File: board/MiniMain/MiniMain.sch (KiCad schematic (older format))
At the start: 40 parts

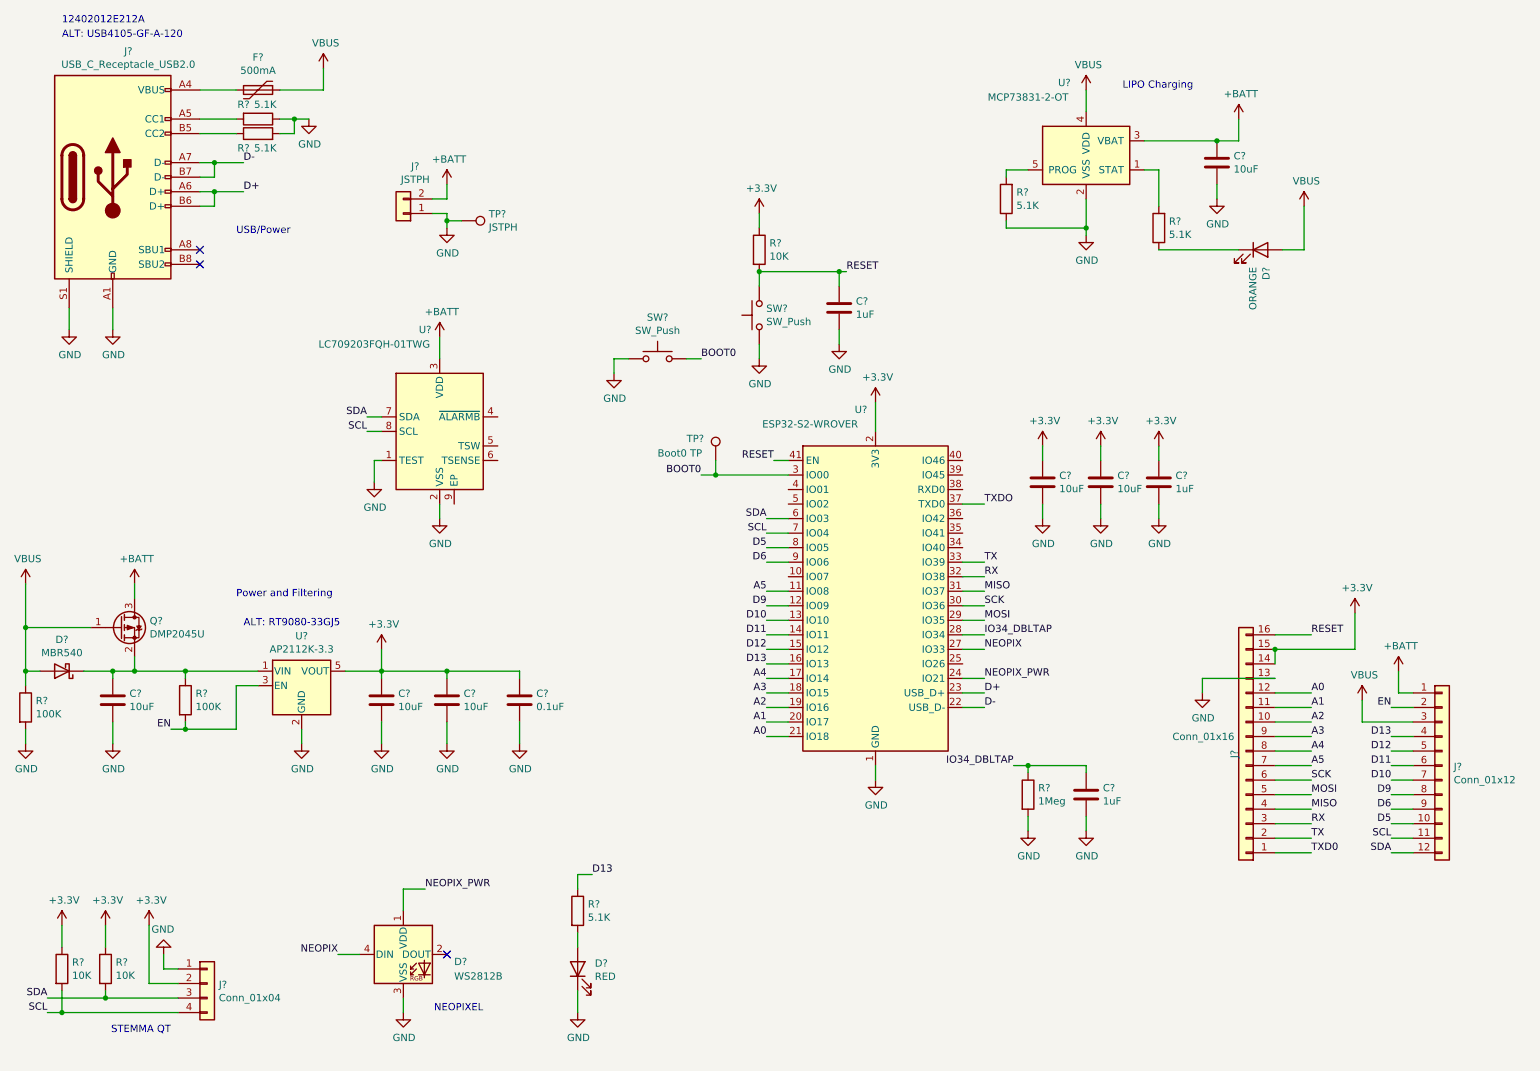
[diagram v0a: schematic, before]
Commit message: Added support for turning power off on the "Stemma QT" port like in the Adafruit esp32-s2 feather.
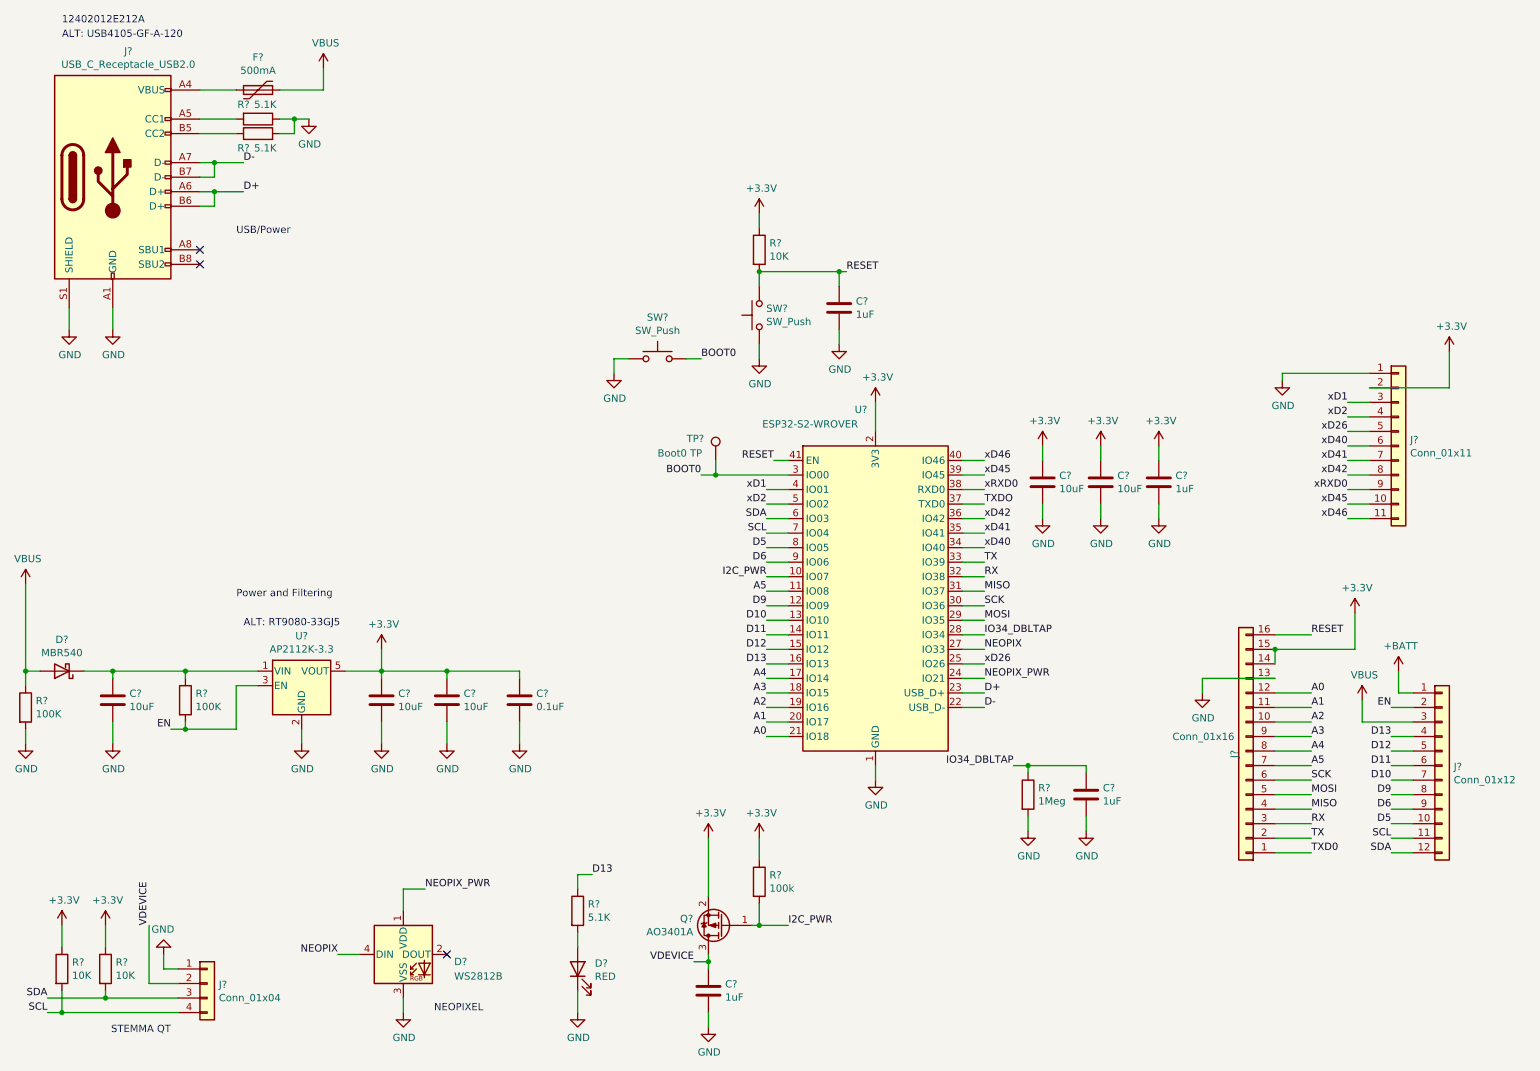
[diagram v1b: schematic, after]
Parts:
- removed C?: 10uF, symbol Device:C
- removed D?: ORANGE, symbol Device:LED
- removed J?: JSTPH, symbol Connector_Generic:Conn_01x02
- removed Q?: DMP2045U, Package_TO_SOT_SMD:SOT-23, symbol Transistor_FET:AO3401A
- removed R? (x2): 5.1K, symbol Device:R
- removed TP?: JSTPH, symbol Connector:TestPoint
- removed U?: LC709203FQH-01TWG, Package_DFN_QFN:WDFN-8-1EP_4x3mm_P0.65mm_EP2.4x1.8mm, symbol Battery_Management:LC709203FQH-01TWG
- removed U?: MCP73831-2-OT, Package_TO_SOT_SMD:SOT-23-5, symbol Battery_Management:MCP73831-2-OT
- added C?: 1uF, symbol Device:C
- added J?: Conn_01x11, symbol Connector_Generic:Conn_01x11
- added Q?: AO3401A, Package_TO_SOT_SMD:SOT-23, symbol Transistor_FET:AO3401A
- added R?: 100k, symbol Device:R
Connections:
- net +3V3: now also J?.2 (Pin_2), Q?.2 (S), R?.1; no longer J?.2 (Pin_2)
- net GND: now also C?.2, J?.1 (Pin_1)
- net I2C_PWR: now reaches U?.10 (IO07)
- net I2C_PWR: now also Q?.1 (G), R?.2
- net xD26: now reaches U?.25 (IO26)
- net xD26: now also J?.5 (Pin_5)
- net xD40: now reaches U?.34 (IO40)
- net xD40: now also J?.6 (Pin_6)
- net xD41: now reaches U?.35 (IO41)
- net xD41: now also J?.7 (Pin_7)
- net xD42: now reaches U?.36 (IO42)
- net xD42: now also J?.8 (Pin_8)
- net xRXD0: now reaches U?.38 (RXD0)
- net xRXD0: now also J?.9 (Pin_9)
- net xD45: now reaches U?.39 (IO45)
- net xD45: now also J?.10 (Pin_10)
- net xD1: now reaches U?.4 (IO01)
- net xD1: now also J?.3 (Pin_3)
- net xD46: now reaches U?.40 (IO46)
- net xD46: now also J?.11 (Pin_11)
- net xD2: now reaches U?.5 (IO02)
- net xD2: now also J?.4 (Pin_4)
- new net VDEVICE: C?.1, J?.2 (Pin_2), Q?.3 (D)
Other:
- note removed: "LIPO Charging"

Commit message: Board layout complete with silkscreen done.
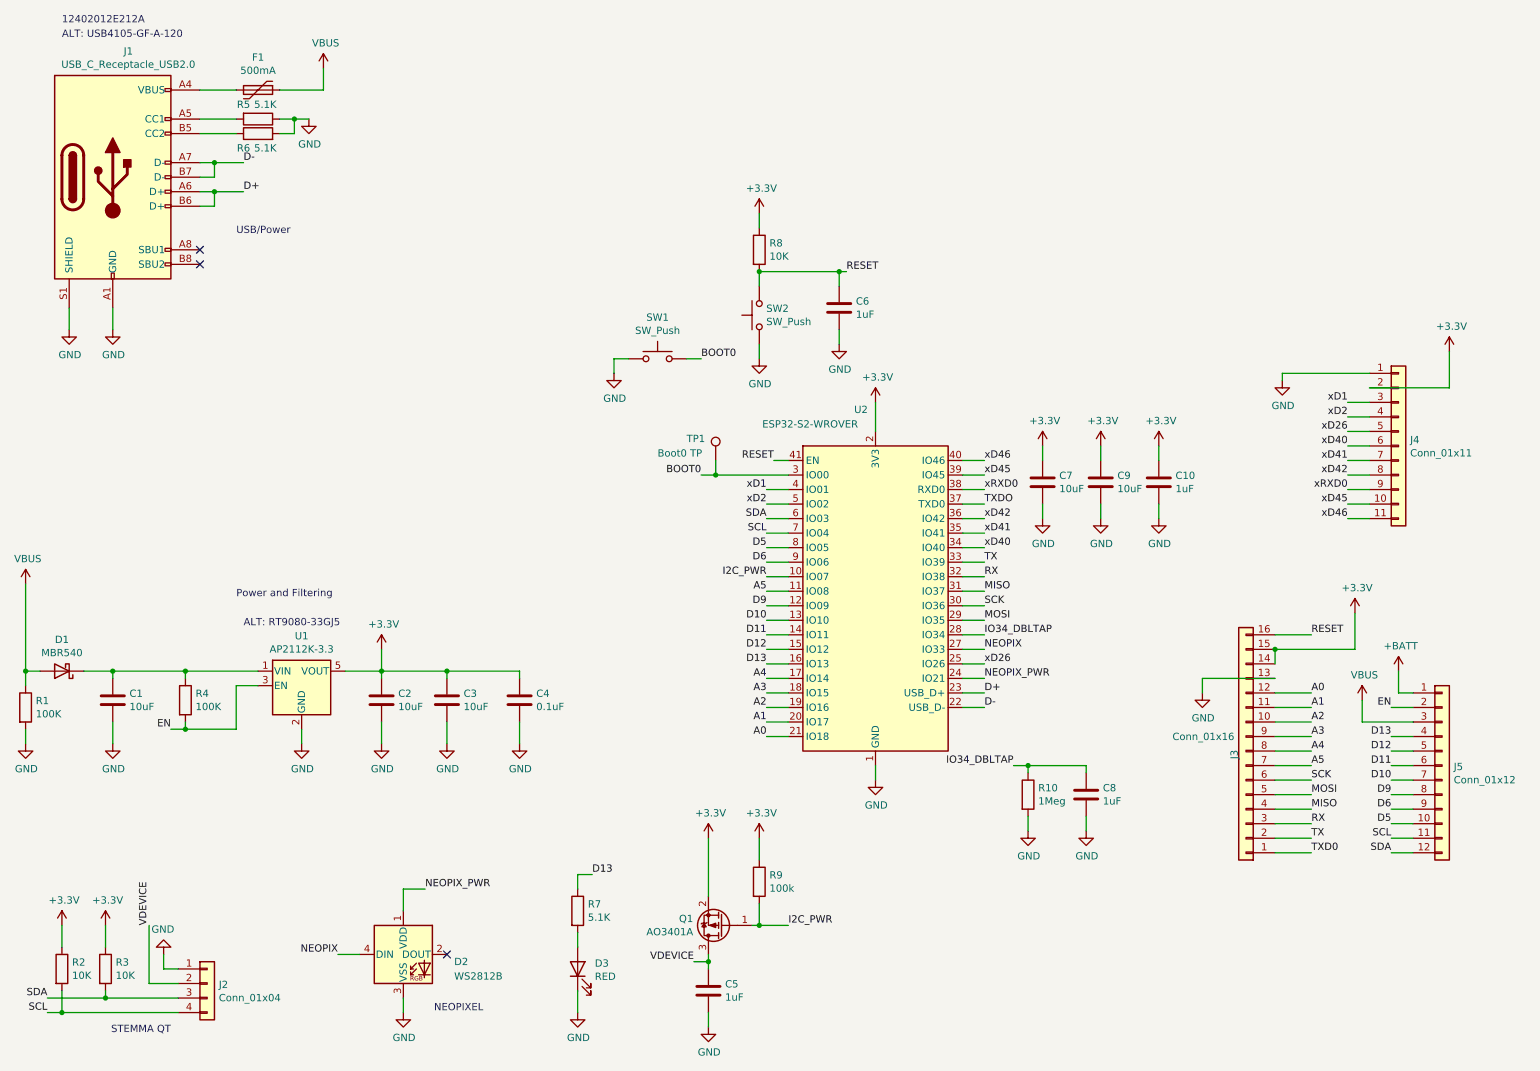
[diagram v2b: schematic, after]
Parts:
- C1, C10, C2, C3, C4, C5, C6, C7, C8, C9: renamed from C?; footprint (none) -> Capacitors_SMD:C_0603_HandSoldering
- D3: renamed from D?; footprint (none) -> LEDs:LED_0603_HandSoldering
- J3: renamed from J?; footprint (none) -> Connector_PinHeader_2.54mm:PinHeader_1x16_P2.54mm_Horizontal
- J4: renamed from J?; footprint (none) -> Connector_PinHeader_2.54mm:PinHeader_1x11_P2.54mm_Vertical
- J5: renamed from J?; footprint (none) -> Connector_PinHeader_2.54mm:PinHeader_1x12_P2.54mm_Vertical
- R1, R10, R2, R3, R4, R5, R6, R7, R8, R9: renamed from R?; footprint (none) -> Resistors_SMD:R_0603_HandSoldering
- SW1, SW2: renamed from SW?; footprint (none) -> Resistors_SMD:R_0603_HandSoldering
- TP1: renamed from TP?; footprint (none) -> Resistors_SMD:R_0603_HandSoldering
- gave numbers to parts that had none: 8
